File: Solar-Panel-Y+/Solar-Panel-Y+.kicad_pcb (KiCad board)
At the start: 6 copper layers, 50 x 50 mm, 64 parts, among them J1 FFC2B28-10-G, U1 TSL2561, U2 Value

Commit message: Exported Gerbers
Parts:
- added H1: MountingHole, MountingHole:MountingHole_2.2mm_M2_DIN965, F.Cu at (84.6, 40.5)
- added H2: MountingHole, MountingHole:MountingHole_2.2mm_M2_DIN965, F.Cu at (84.6, 80.3)
- added H3: MountingHole, MountingHole:MountingHole_2.2mm_M2_DIN965, F.Cu at (124.4, 80.3)
- added H4: MountingHole, MountingHole:MountingHole_2.2mm_M2_DIN965, F.Cu at (124.4, 40.5)
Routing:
- net /coil: track 12938.3 -> 12382.5 mm
- net Net-(C10-Pad1): track 8.82 -> 7.78 mm
- net GND: track 7.13 -> 6.33 mm
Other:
- outline, holes or cut-outs redrawn

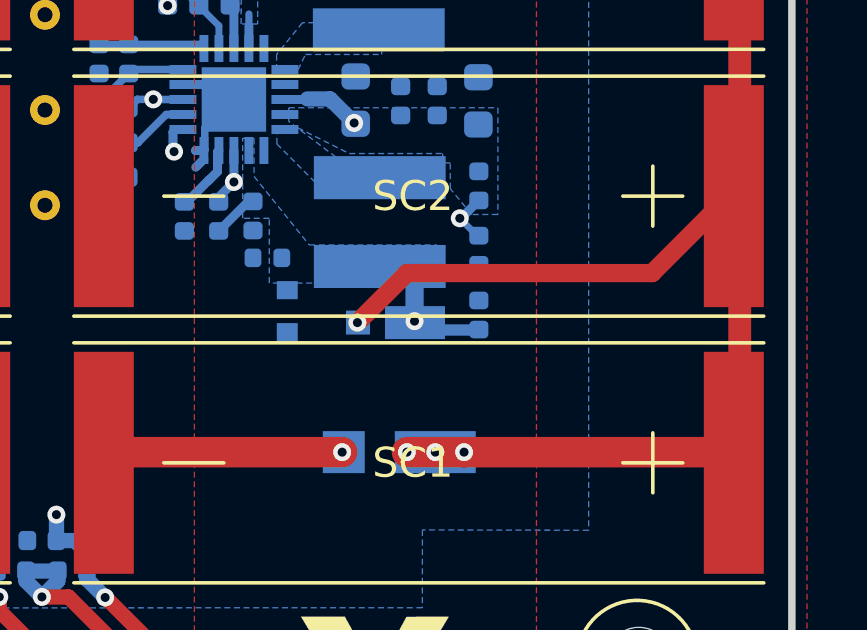
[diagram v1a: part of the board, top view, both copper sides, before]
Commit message: Stack architecture schematic updates / fixes
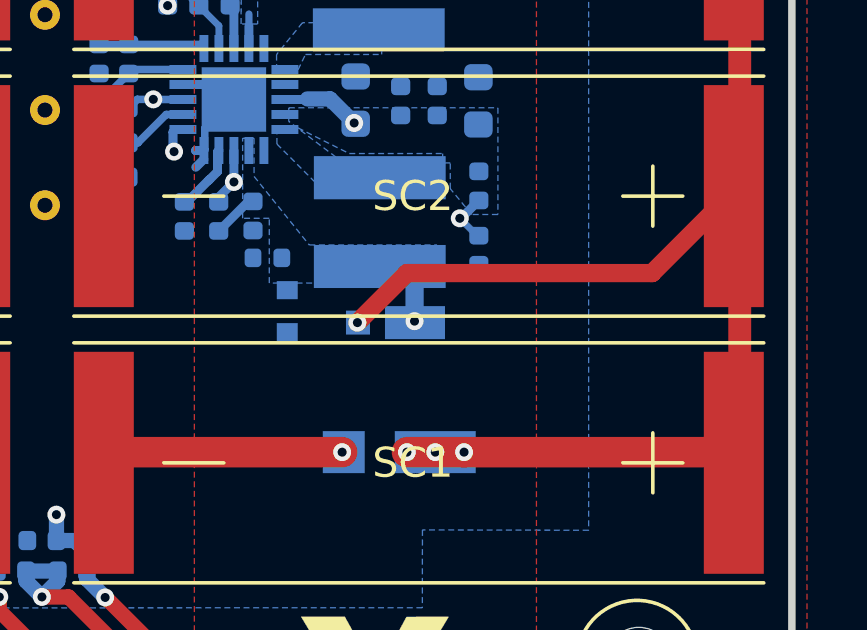
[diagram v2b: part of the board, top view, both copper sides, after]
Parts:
- removed the C4 at (119.1, 68.8)
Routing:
- net VSOLAR: track 20.2 -> 18.3 mm
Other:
- board text removed: "v00"
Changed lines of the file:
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@@
   )
   (footprint "Capacitor_SMD:C_0402_1005Metric" (layer "B.Cu")
-    (at 119.09076 68.834 90)
-    (descr "Capacitor SMD 0402 (1005 Metric), square (rectangular) end terminal, IPC_7351 nominal, (Body size source: http://www.tortai-tech.com/upload/download/2011102023233369053.pdf), generated with kicad-footprint-generator")
-    (tags "capacitor")
-    (attr smd)
-    (fp_text reference "C4" (at 0 0.98044 90) (layer "B.SilkS")
-      (effects (font (size 0.381 0.381) (thickness 0.0762)) (justify mirror))
-    )
-    (fp_text value "0.1uF" (at 0 -1.17 90) (layer "B.Fab")
-      (effects (font (size 1 1) (thickness 0.15)) (justify mirror))
-    )
-    (fp_text user "${REFERENCE}" (at 0 0 90) (layer "B.Fab")
-      (effects (font (size 0.889 0.889) (thickness 0.127)) (justify mirror))
-    )
-    (fp_line (start 0.93 -0.47) (end -0.93 -0.47) (layer "B.CrtYd") (width 0.05))
-    (fp_line (start -0.93 -0.47) (end -0.93 0.47) (layer "B.CrtYd") (width 0.05))
-    (fp_line (start 0.93 0.47) (end 0.93 -0.47) (layer "B.CrtYd") (width 0.05))
-    (fp_line (start -0.93 0.47) (end 0.93 0.47) (layer "B.CrtYd") (width 0.05))
-    (fp_line (start 0.5 0.25) (end 0.5 -0.25) (layer "B.Fab") (width 0.1))
-    (fp_line (start 0.5 -0.25) (end -0.5 -0.25) (layer "B.Fab") (width 0.1))
-    (fp_line (start -0.5 -0.25) (end -0.5 0.25) (layer "B.Fab") (width 0.1))
-    (fp_line (start -0.5 0.25) (end 0.5 0.25) (layer "B.Fab") (width 0.1))
-    (pad "1" smd roundrect locked (at -0.485 0 90) (size 0.59 0.64) (layers "B.Cu" "B.Paste" "B.Mask") (roundrect_rratio 0.25)
-      (net 6 "VSOLAR"))
-    (pad "2" smd roundrect locked (at 0.485 0 90) (size 0.59 0.64) (layers "B.Cu" "B.Paste" "B.Mask") (roundrect_rratio 0.25)
-      (net 4 "GND"))
-    (model "${KISYS3DMOD}/Capacitor_SMD.3dshapes/C_0402_1005Metric.step"
-      (offset (xyz 0 0 0))
-      (scale (xyz 1 1 1))
-      (rotate (xyz 0 0 0))
-    )
-  )
-  (footprint "Capacitor_SMD:C_0402_1005Metric" (layer "B.Cu")
     (at 111.5622 65.532 -90)
     (descr "Capacitor SMD 0402 (1005 Metric), square (rectangular) end terminal, IPC_7351 nominal, (Body size source: http://www.tortai-tech.com/upload/download/2011102023233369053.pdf), generated with kicad-footprint-generator")
@@
     (effects (font (size 0.889 0.889) (thickness 0.15)))
   )
-  (gr_text "v00" (at 346.2655 218.059) (layer "B.Mask")
-    (effects (font (size 1.5 1.5) (thickness 0.3)) (justify mirror))
-  )
   (gr_text "v03" (at 104.7804 82.55) (layer "B.Mask")
     (effects (font (size 1.016 1.016) (thickness 0.2032)) (justify mirror))
   )
-  (gr_text "v00" (at 346.5195 218.059) (layer "F.Mask")
-    (effects (font (size 1.5 1.5) (thickness 0.3)))
-  )
   (gr_text "v03" (at 118.725 83.1596) (layer "F.Mask")
     (effects (font (size 1.27 1.27) (thickness 0.254)))
@@
   (segment (start 109.5302 66.929) (end 104.628 62.0268) (width 0.6096) (layer "In2.Cu") (net 6))
   (segment (start 116.947 69.03974) (end 114.83626 66.929) (width 0.6096) (layer "In2.Cu") (net 6))
-  (segment (start 118.88756 69.33424) (end 117.03806 69.33424) (width 0.381) (layer "B.Cu") (net 6))
   (segment (start 111.4122 65.047) (end 110.4192 66.04) (width 0.29972) (layer "B.Cu") (net 6))
   (segment (start 116.947 69.03974) (end 116.947 67.34048) (width 0.6096) (layer "B.Cu") (net 6))

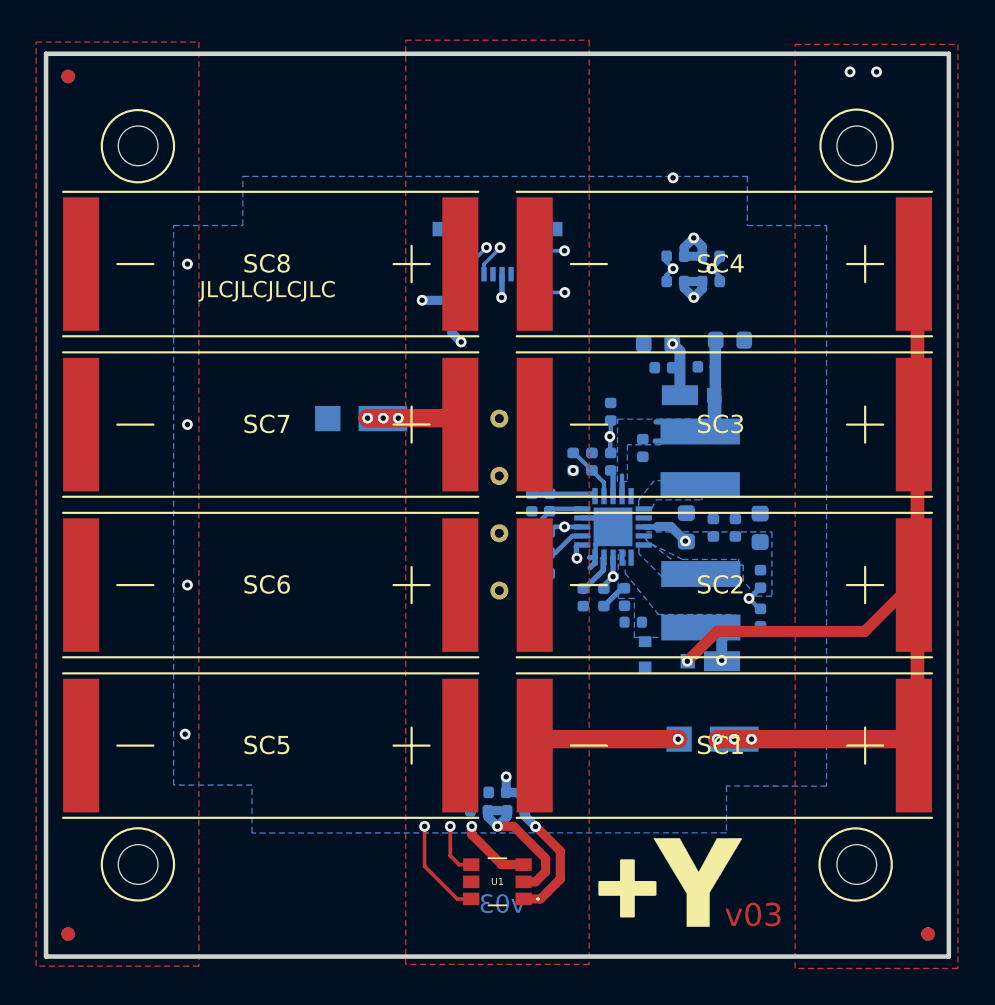
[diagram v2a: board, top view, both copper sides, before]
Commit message: X / Y+ board updates v04
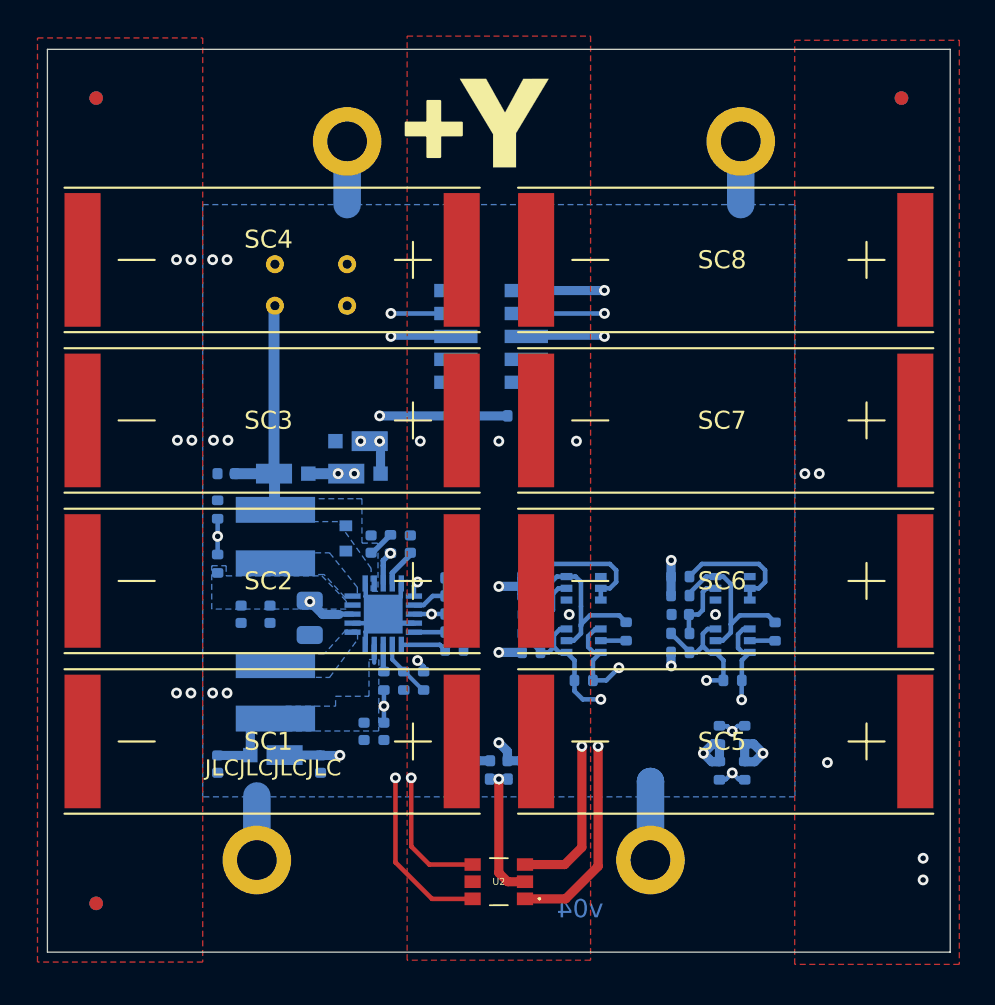
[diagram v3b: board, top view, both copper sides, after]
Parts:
- removed C14: 100uF, Capacitor_SMD:C_0603_1608Metric
- removed the C5 at (112.0, 66.9)
- removed the C8 at (116.5, 61.7)
- removed the D5 at (112.7, 68.7)
- removed R4: 0, Resistor_SMD:R_0402_1005Metric
- removed the R5 at (102.0, 49.6)
- added C2: 0.1uF, Capacitor_SMD:C_0402_1005Metric, B.Cu at (89.5, 58.7)
- added C7: 4.7uF, Capacitor_SMD:C_0402_1005Metric, B.Cu at (91.9, 66.5)
- added D3: MSS1P4-M3_89A, solarpanels:MICROSMP, B.Cu at (96.8, 56.9)
- added Q1: BSS138DWQ-7, Package_TO_SOT_SMD:SOT-363_SC-70-6, B.Cu at (109.3, 65.0)
- added Q2: MBT2222ADW1T1, Package_TO_SOT_SMD:SOT-363_SC-70-6, B.Cu at (109.3, 68.0)
- added Q3: BSS138DWQ-7, Package_TO_SOT_SMD:SOT-363_SC-70-6, B.Cu at (117.5, 65.0)
- added Q4: MBT2222ADW1T1, Package_TO_SOT_SMD:SOT-363_SC-70-6, B.Cu at (117.5, 68.0)
- added R20: 680, Resistor_SMD:R_0402_1005Metric, B.Cu at (111.7, 67.4)
- added R21: 100K, Resistor_SMD:R_0402_1005Metric, B.Cu at (106.4, 64.4)
- added R22: 0, Resistor_SMD:R_0402_1005Metric, B.Cu at (109.3, 70.1)
- added R23: 0, Resistor_SMD:R_0402_1005Metric, B.Cu at (117.5, 70.2)
- added R24: 10K, Resistor_SMD:R_0402_1005Metric, B.Cu at (106.4, 65.5)
- added R25: 10K, Resistor_SMD:R_0402_1005Metric, B.Cu at (106.4, 68.6)
- added R26: 200K, Resistor_SMD:R_0402_1005Metric, B.Cu at (106.4, 67.5)
- added R27: 680, Resistor_SMD:R_0402_1005Metric, B.Cu at (119.9, 67.5)
- added R28: 100K, Resistor_SMD:R_0402_1005Metric, B.Cu at (114.7, 64.4)
- added R29: 10K, Resistor_SMD:R_0402_1005Metric, B.Cu at (114.7, 65.5)
- added R3: 0, Resistor_SMD:R_0402_1005Metric, B.Cu at (105.6, 55.5)
- added R30: 10K, Resistor_SMD:R_0402_1005Metric, B.Cu at (114.7, 68.6)
- added R31: 200K, Resistor_SMD:R_0402_1005Metric, B.Cu at (114.7, 67.5)
- C11: value 100uF -> 0.1uF; footprint Capacitor_SMD:C_0603_1608Metric -> Capacitor_SMD:C_0402_1005Metric
- C12: value 100uF -> 10nF; footprint Capacitor_SMD:C_0603_1608Metric -> Capacitor_SMD:C_0402_1005Metric
- C13: value 0.1uF -> 10nF
- C5: renamed from C6; footprint Capacitor_SMD:C_0603_1608Metric -> Capacitor_SMD:C_0805_2012Metric
- C6: renamed from C2; value 1.0uF -> 1uF
- D1: value SBDiode -> SZMM5Z5V1T1G; footprint solarpanels:SB Diode -> Diode_SMD:D_SOD-523
- D2: value SBDiode -> MSS1P4-M3_89A; footprint solarpanels:SB Diode -> solarpanels:MICROSMP
- H1, H2, H3, H4: footprint MountingHole:MountingHole_2.2mm_M2_DIN965 -> MountingHole:MountingHole_2.2mm_M2_DIN965_Pad
- J1: value FFC2B28-10-G -> TODO; footprint solarpanels:GCT_FFC2B28-10-G -> Connector_PinHeader_1.27mm:PinHeader_2x05_P1.27mm_Vertical_SMD
- moved REF** 46.3 mm to (82.3, 37.9), turned to 180 degrees (x2)
- moved REF** 46.2 mm to (126.9, 37.9), turned to 180 degrees (x2)
- moved REF** 46.1 mm to (82.3, 82.5), turned to 180 degrees (x2)
- moved Ref** 43.4 mm to (121.9, 40.2)
- moved H2 41.7 mm to (96.2, 40.3), turned to -90 degrees
- moved H4 41.2 mm to (113.0, 80.1), turned to -90 degrees
- moved C10 34.9 mm to (89.0, 74.8), turned to -90 degrees
- moved H1 33.4 mm to (118.0, 40.3), turned to -90 degrees
- moved H3 33.2 mm to (91.2, 80.1), turned to -90 degrees
- moved R15 30.7 mm to (89.0, 60.7), turned to -90 degrees
- moved R16 30.1 mm to (89.0, 63.7), turned to 90 degrees
- moved R13 28.5 mm to (118.2, 75.1), turned to -90 degrees
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- renumbered C7 to C8, D3 to D5, R12 to R10, R3 to R12, R8 to R13, R6 to R14, R7 to R15, R14 to R16, R9 to R17, R10 to R18, R13 to R19, R15 to R5, R16 to R6, R17 to R7, R18 to R8, R19 to R9, SC5 to SC1, SC6 to SC2, SC7 to SC3, SC8 to SC4, SC1 to SC5, SC2 to SC6, SC3 to SC7, SC4 to SC8, U2 to U1, U1 to U2
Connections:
- C11 pad 1: Net-(C11-Pad1) -> +3V3
- C12 pad 1: Net-(C10-Pad1) -> Net-(C12-Pad1)
- C13 pad 1: +3V3 -> Net-(C13-Pad1)
- C5 pad 1: /VBAT -> VBAT
- C9 pad 1: Net-(C11-Pad1) -> Net-(C7-Pad1)
- D1 pad 1: Net-(D1-Pad1) -> VSOLAR
- D1 pad 2: Net-(D1-Pad2) -> GND
- D2 pad 1: Net-(D1-Pad2) -> +3V3
- D2 pad 2: GND -> Net-(C10-Pad1)
- D4 pad 1: +3V3 -> Net-(D4-Pad1)
- D4 pad 2: Net-(C10-Pad1) -> Net-(D3-Pad1)
- D5 pad 2: Net-(D1-Pad1) -> Net-(D4-Pad1)
- J1 pad 1: BATT_P -> +3V3
- J1 pad 10: COIL_P -> VUSB
- J1 pad 2: BATT_N -> GND
- J1 pad 3: SDA1 -> SDA3
- J1 pad 4: SCL1 -> SCL3
- J1 pad 5: BURN1 -> COIL_P
- J1 pad 6: +3V3 -> COIL_N
- J1 pad 7: GND -> BURN1
- J1 pad 8: GND -> BURN2
- J1 pad 9: COIL_N -> BATT_P
- R16 pad 1: Net-(C11-Pad1) -> Net-(C7-Pad1)
- SC1 pad 1: Net-(D1-Pad2) -> Net-(D3-Pad1)
- SC2 pad 1: Net-(D1-Pad2) -> Net-(D3-Pad1)
- SC3 pad 1: Net-(D1-Pad2) -> Net-(D3-Pad1)
- SC4 pad 1: Net-(D1-Pad2) -> Net-(D3-Pad1)
- SC5 pad 1: Net-(D1-Pad1) -> Net-(D4-Pad1)
- SC5 pad 2: Net-(D1-Pad2) -> Net-(D3-Pad1)
- SC6 pad 1: Net-(D1-Pad1) -> Net-(D4-Pad1)
- SC6 pad 2: Net-(D1-Pad2) -> Net-(D3-Pad1)
- SC7 pad 1: Net-(D1-Pad1) -> Net-(D4-Pad1)
- SC7 pad 2: Net-(D1-Pad2) -> Net-(D3-Pad1)
- SC8 pad 1: Net-(D1-Pad1) -> Net-(D4-Pad1)
- SC8 pad 2: Net-(D1-Pad2) -> Net-(D3-Pad1)
- TP2 pad 1: +3V3 -> GND
- TP3 pad 1: GND -> +3V3
- TP4 pad 1: BATT_P -> VBAT
- U1 pad 18: /VBAT -> VBAT
- U1 pad 19: Net-(C11-Pad1) -> Net-(C7-Pad1)
- U2 pad 4: SCL1 -> SCL_LS
- U2 pad 6: SDA1 -> SDA_LS
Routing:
- net /coil: track 12382.5 -> 12253.1 mm
- net Net-(D1-Pad1): track 52.4 -> 0.00 mm, vias 4 -> 0
- net SDA1: track 40.8 -> 0.00 mm, vias 2 -> 0
- net VBAT: track 0.00 -> 39.9 mm, vias 0 -> 2
- net SCL3: track 0.00 -> 38.5 mm, vias 0 -> 2
- net SCL1: track 38.3 -> 0.00 mm, vias 2 -> 0
- net SDA_LS: track 0.00 -> 37.5 mm, vias 0 -> 2
- net GND: track 6.33 -> 41.9 mm, vias 5 -> 15
- net SDA3: track 0.00 -> 35.5 mm, vias 0 -> 2
- net COIL_N: track 13.3 -> 46.1 mm
- net Net-(D4-Pad1): track 0.00 -> 29.1 mm, vias 0 -> 4
- net SCL_LS: track 0.00 -> 29.0 mm, vias 0 -> 2
- net +3V3: track 53.2 -> 28.2 mm, vias 4 -> 8
- net /VBAT: track 24.3 -> 0.00 mm, vias 2 -> 0
- net COIL_P: track 13.4 -> 35.8 mm
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- added copper zone on In2.Cu, net +3V3
- added copper zone on In3.Cu, net GND
- added copper zone on B.Cu, net Net-(C7-Pad1)
- added copper zone on F.Cu, net Net-(D3-Pad1)
- added copper zone on F.Cu, net Net-(D4-Pad1)
- removed copper zone on B.Cu, net Net-(C11-Pad1)
- removed copper zone on F.Cu, net Net-(D1-Pad1)
- removed copper zone on F.Cu, net Net-(D1-Pad2)
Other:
- board text added: "Cable Pinout 1.BATT_P 2.VUSB 3.BURN1 4.BURN2 5.COIL_P 6.COIL_N 7.SDA 8.SCL 9.+3V3 10.GND"
- board text added: "v04"
- board text removed: "1"
- board text removed: "Cable Pinout 1.BATT_P 2.BATT_N 3.SDA 4.SCL 5.BURN 6.3V3 7.GND 8.GND 9.COIL_N 10.COIL_P"
- board text removed: "v03"

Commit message: Re-check boards, fixed connector pinouts, moved Y+ connector, re-export models
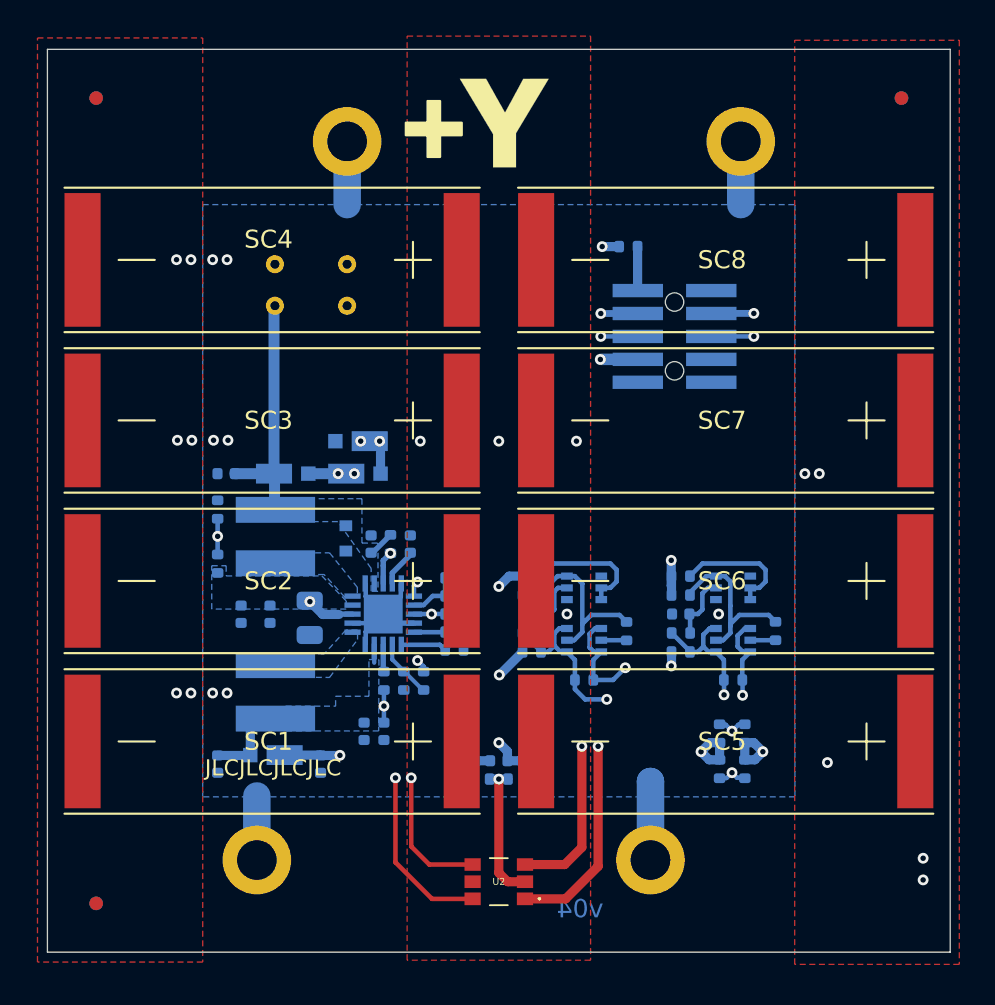
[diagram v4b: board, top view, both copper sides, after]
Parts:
- J1: value TODO -> FTS-105-01-L-DV-A; footprint Connector_PinHeader_1.27mm:PinHeader_2x05_P1.27mm_Vertical_SMD -> batteryboard:FTS-105-XX-YY-DV-A
- moved R3 11.2 mm to (111.8, 46.1)
- moved J1 10.2 mm to (114.3, 51.1), turned to 90 degrees
- moved Q1 8.28 mm to (117.6, 65.0)
- moved Q2 8.28 mm to (117.6, 67.9)
- moved R22 8.28 mm to (117.6, 70.1)
- moved R26 8.28 mm to (114.7, 67.5)
- moved C12 8.28 mm to (114.7, 66.5)
- moved R20 8.28 mm to (119.9, 67.4)
- moved R21 8.28 mm to (114.7, 64.4)
- moved R24 8.28 mm to (114.7, 65.4)
- moved R25 8.28 mm to (114.7, 68.6)
- moved C13 8.23 mm to (106.4, 66.5)
- moved R27 8.23 mm to (111.7, 67.4)
- moved R28 8.23 mm to (106.4, 64.4)
- moved R29 8.23 mm to (106.4, 65.4)
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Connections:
- net VUSB renamed VBUS
- J1 pad 1: +3V3 -> unconnected-(J1-Pad1)
- J1 pad 2: GND -> unconnected-(J1-Pad2)
- J1 pad 3: SDA3 -> +3V3
- J1 pad 4: SCL3 -> GND
- J1 pad 5: COIL_P -> SDA3
- J1 pad 6: COIL_N -> SCL3
- J1 pad 7: BURN1 -> COIL_P
- J1 pad 8: BURN2 -> COIL_N
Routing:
- net COIL_N: track 46.1 -> 32.1 mm
- net SCL3: track 38.5 -> 27.4 mm
- net VBAT: track 39.9 -> 50.0 mm
- net SDA3: track 35.5 -> 27.0 mm
- net SCL_LS: track 29.0 -> 34.7 mm
- net SDA_LS: track 37.5 -> 33.1 mm
- net COIL_P: track 35.8 -> 32.0 mm
- net +3V3: track 28.2 -> 27.3 mm
- net BATT_P: track 1.87 -> 2.44 mm

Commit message: New X board keepouts
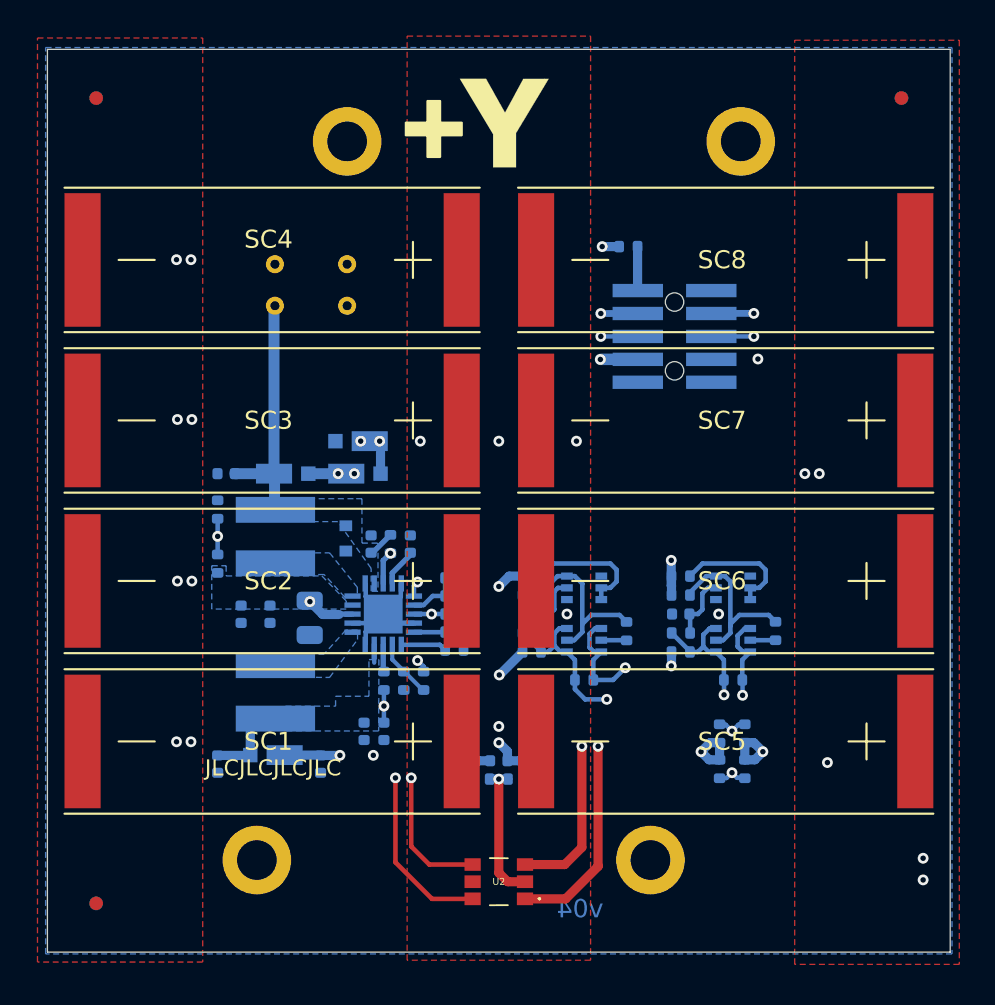
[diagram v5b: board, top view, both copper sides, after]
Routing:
- net GND: track 41.9 -> 17.9 mm, vias 15 -> 14
- added copper zone on In1.Cu, net +3V3
- added copper zone on In4.Cu, net GND
